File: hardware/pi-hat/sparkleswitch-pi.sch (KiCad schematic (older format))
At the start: 21 parts, among them J1 Conn_01x02, J2 Conn_02x06_Odd_Even, P1 CONN_02X20, U1 74HCT245, U2 74HCT245, U3 74HCT245, U4 PC817, U5 PC817, U6 PC817, U7 PC817

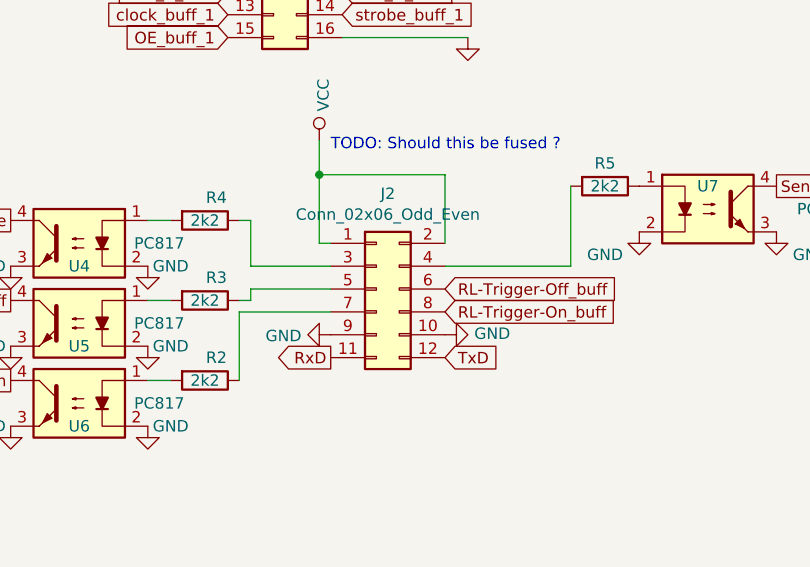
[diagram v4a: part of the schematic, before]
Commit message: Use 4.7k for OptoCoupler LEDs; OE-Pullup 0805 -> 0603
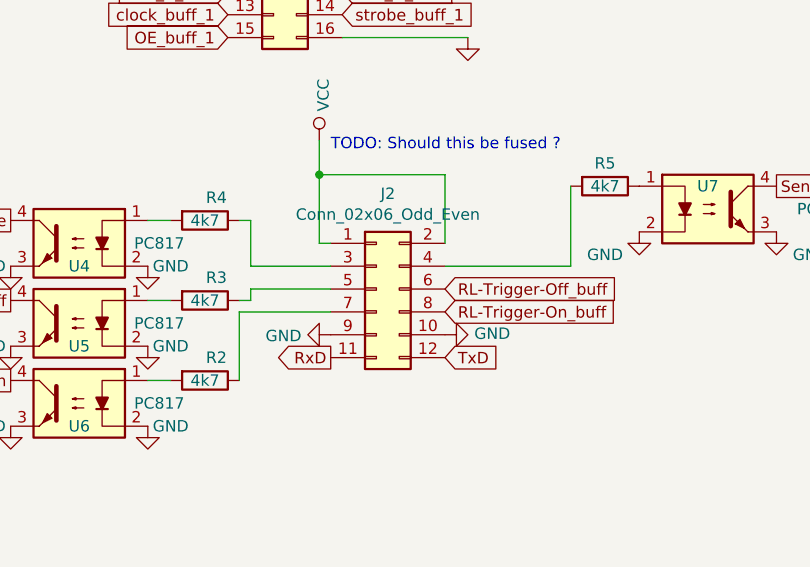
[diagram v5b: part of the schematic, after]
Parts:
- R1: footprint Resistors_SMD:R_0805_HandSoldering -> Resistors_SMD:R_0603
- R2, R3, R4, R5: value 2k2 -> 4k7
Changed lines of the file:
@@
 F 0 "R1" V 3080 2450 50  0000 C CNN
 F 1 "10k" V 3000 2450 50  0000 C CNN
-F 2 "Resistors_SMD:R_0805_HandSoldering" V 2930 2450 30  0001 C CNN
+F 2 "Resistors_SMD:R_0603" V 2930 2450 30  0001 C CNN
 F 3 "" H 3000 2450 30  0000 C CNN
 	1    3000 2450
@@
 P 9900 4800
 F 0 "R5" V 9800 4800 50  0000 C CNN
-F 1 "2k2" V 9900 4800 50  0000 C CNN
+F 1 "4k7" V 9900 4800 50  0000 C CNN
 F 2 "Resistors_SMD:R_0603" V 9830 4800 50  0001 C CNN
 F 3 "" H 9900 4800 50  0001 C CNN
@@
 P 8150 4950
 F 0 "R4" V 8050 5000 50  0000 C CNN
-F 1 "2k2" V 8150 4950 50  0000 C CNN
+F 1 "4k7" V 8150 4950 50  0000 C CNN
 F 2 "Resistors_SMD:R_0603" V 8080 4950 50  0001 C CNN
 F 3 "" H 8150 4950 50  0001 C CNN
@@
 P 8150 5300
 F 0 "R3" V 8050 5350 50  0000 C CNN
-F 1 "2k2" V 8150 5300 50  0000 C CNN
+F 1 "4k7" V 8150 5300 50  0000 C CNN
 F 2 "Resistors_SMD:R_0603" V 8080 5300 50  0001 C CNN
 F 3 "" H 8150 5300 50  0001 C CNN
@@
 P 8150 5650
 F 0 "R2" V 8050 5700 50  0000 C CNN
-F 1 "2k2" V 8150 5650 50  0000 C CNN
+F 1 "4k7" V 8150 5650 50  0000 C CNN
 F 2 "Resistors_SMD:R_0603" V 8080 5650 50  0001 C CNN
 F 3 "" H 8150 5650 50  0001 C CNN
